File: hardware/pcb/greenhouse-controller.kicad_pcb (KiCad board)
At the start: 2 copper layers, 208 x 132 mm, 72 parts, among them J1 Motor 2, J10 ALARM contact, J11 AC-Mains, J12 DM1AA-SF-PEJ72, J2 24V in, J3 I2C Display, J4 Keypad, J5 MODBUS RS485 S200, J6 Motor 3, J7 Motor 1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

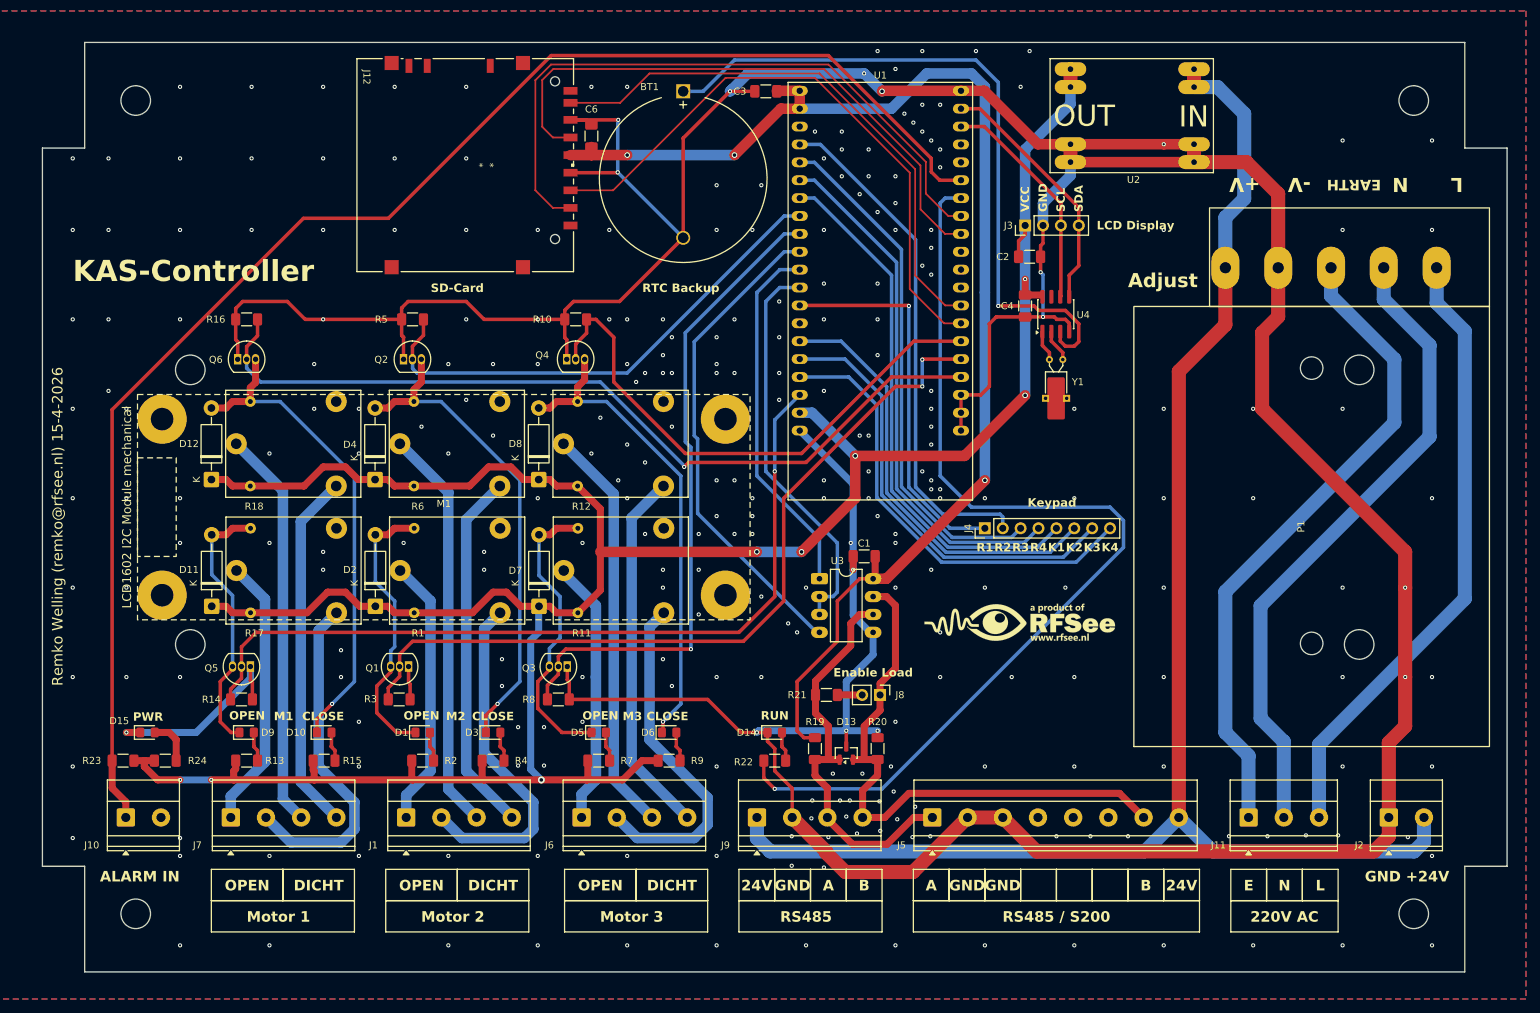
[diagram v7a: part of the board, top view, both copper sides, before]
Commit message: Update LCD and GUI designs, and preliminary changes to implement physical limitation of housing to PCB
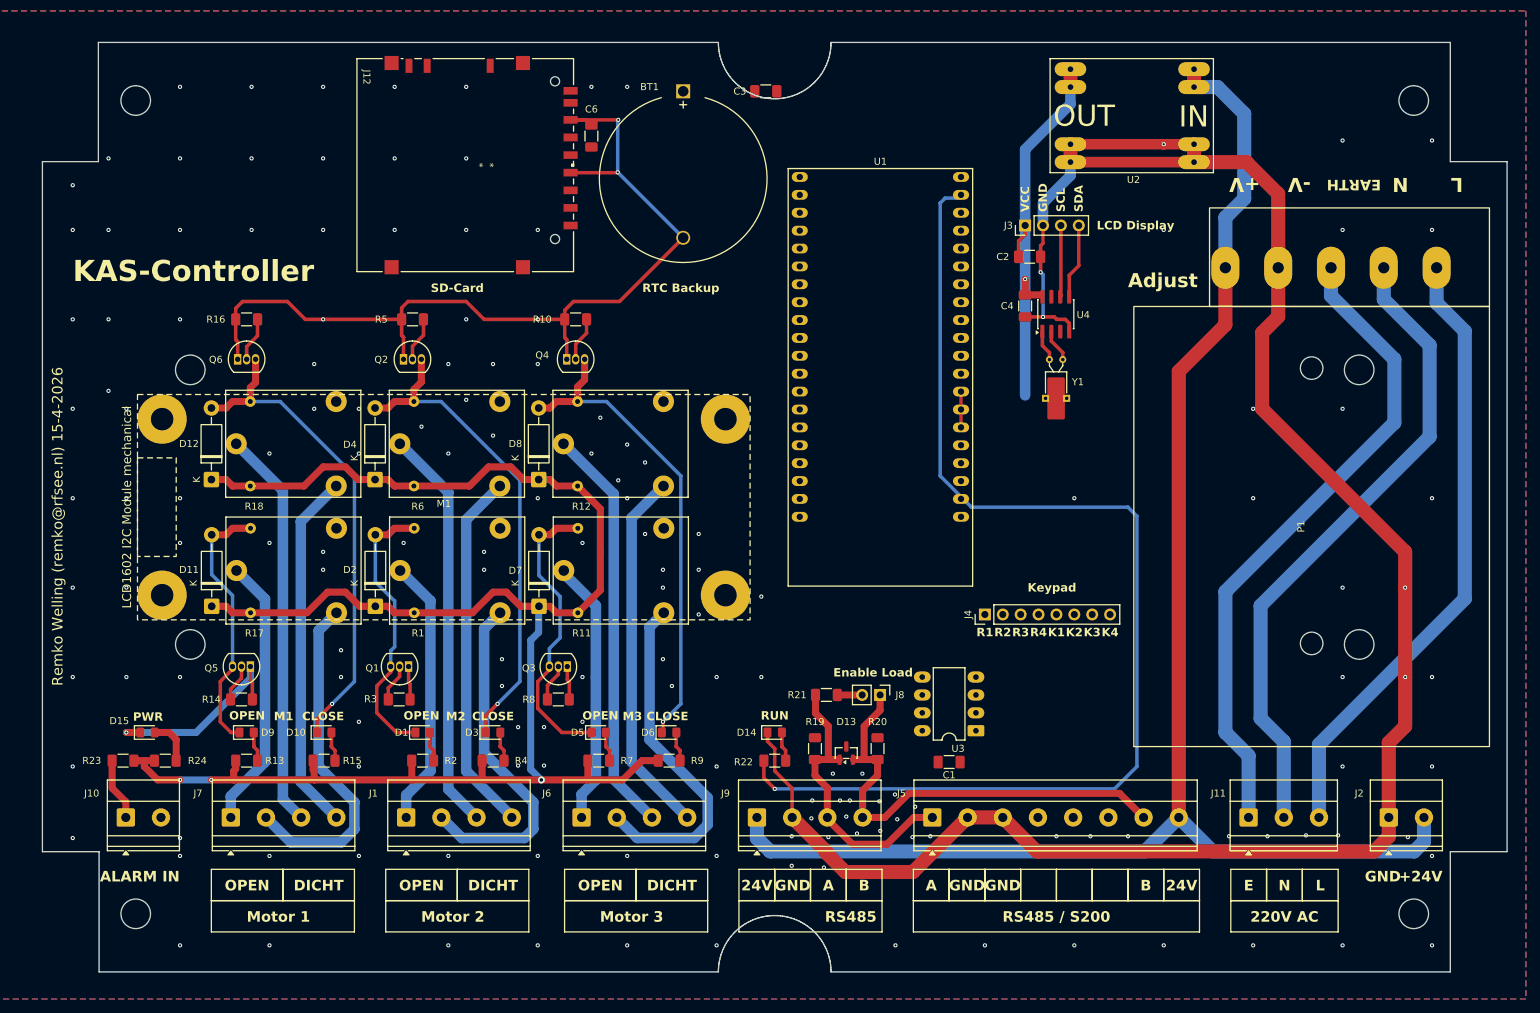
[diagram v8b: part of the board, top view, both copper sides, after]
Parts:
- removed the G*** at (182.8, 106.6)
- moved C1 31.6 mm to (172.7, 126.4), turned to 180 degrees
- moved U3 31.0 mm to (176.5, 121.9), turned to 180 degrees
- moved J4 12.2 mm to (177.8, 105.4)
- moved U1 12.2 mm to (163.0, 67.4)
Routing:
- net /GND: track 670.1 -> 468.8 mm, vias 282 -> 164
- net /OPTO_INPUT: track 208.6 -> 8.87 mm
- net /3V3: track 182.4 -> 0.00 mm, vias 3 -> 0
- net /RELAY_M1_CLOSE: track 120.2 -> 6.31 mm, vias 1 -> 0
- net /RELAY_M1_OPEN: track 116.9 -> 5.31 mm, vias 1 -> 0
- net /RELAY_M2_OPEN: track 115.0 -> 5.34 mm, vias 2 -> 0
- net Net-(BT1-+): track 99.2 -> 0.00 mm, vias 1 -> 0
- net /SD_CS: track 94.6 -> 0.00 mm
- net /RELAY_M3_OPEN: track 93.3 -> 5.31 mm, vias 1 -> 0
- net /SD_MOSI: track 86.2 -> 0.00 mm
- net /SD_CLK: track 84.7 -> 0.00 mm
- net /5V: track 395.4 -> 311.9 mm, vias 8 -> 4
- net /SD_MISO: track 79.7 -> 0.00 mm
- net /KP_COL1: track 76.1 -> 0.00 mm
- net /KP_ROW4: track 74.9 -> 0.00 mm
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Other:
- outline, holes or cut-outs redrawn
